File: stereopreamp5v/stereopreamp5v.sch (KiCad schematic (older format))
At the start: 28 parts, among them J1 Conn_Coaxial, J2 Conn_Coaxial, J3 Conn_Coaxial, J4 Conn_Coaxial, U1 TL072

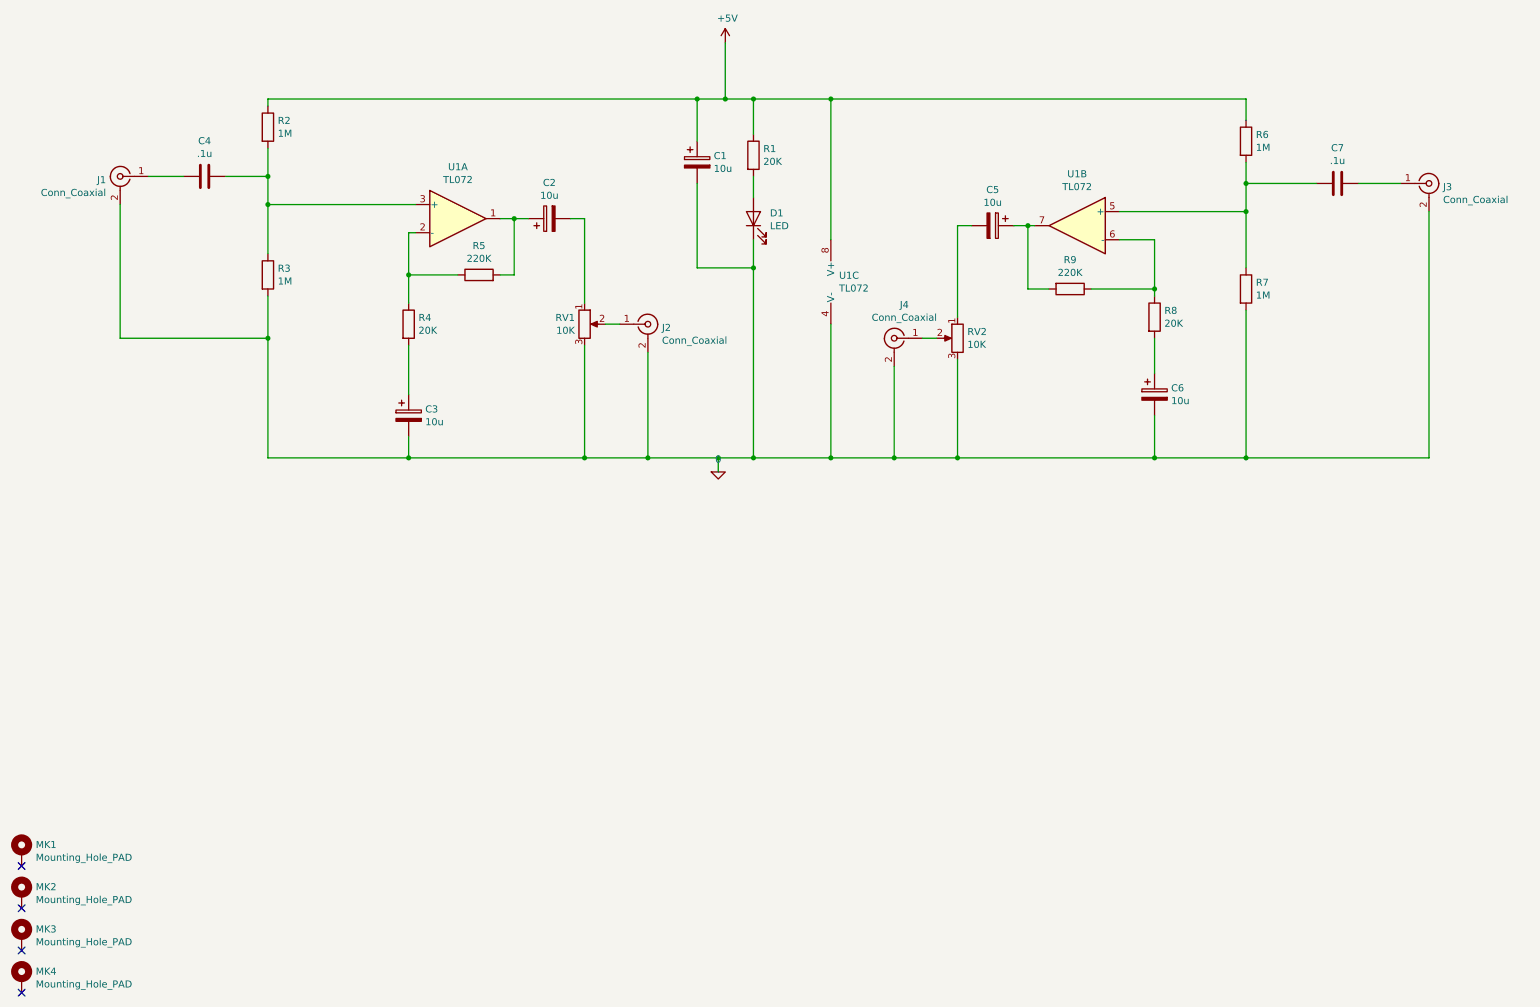
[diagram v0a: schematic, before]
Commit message: replaced input connector
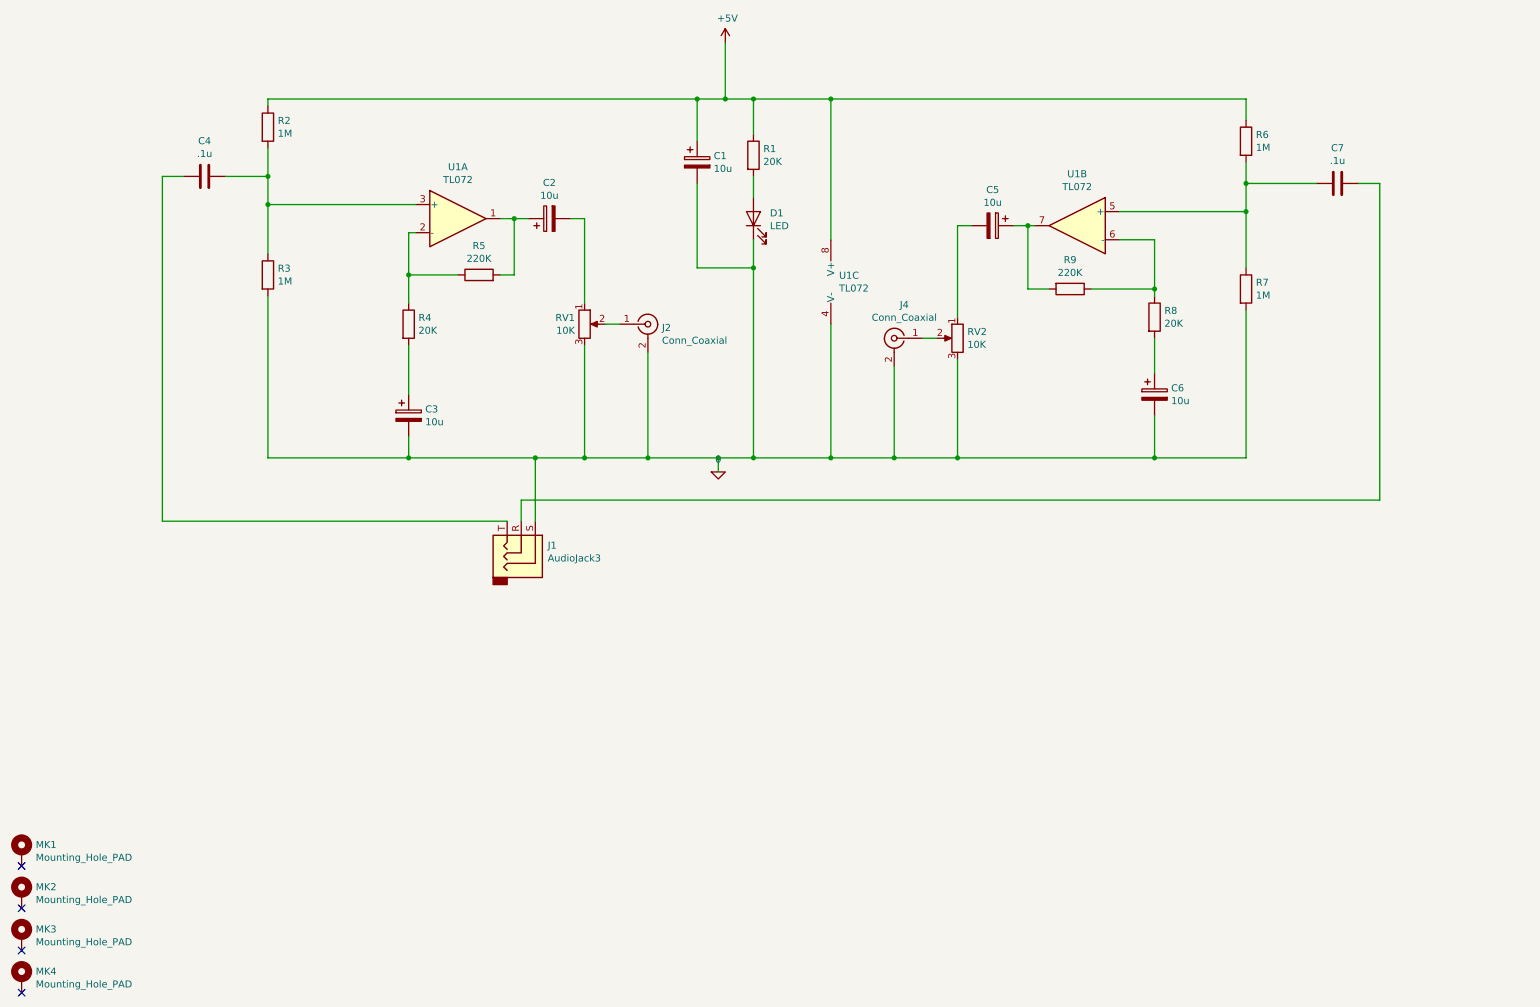
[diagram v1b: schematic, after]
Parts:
- removed J1, J3: Conn_Coaxial, symbol Connector:Conn_Coaxial
- added J1: AudioJack3, symbol Connector:AudioJack3
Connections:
- net 0: now also J1.S
- net at C4.1: now also J1.T
- net at C7.1: now also J1.R
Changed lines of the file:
@@
 NoConn ~ 650  7700
-$Comp
-L Connector:Conn_Coaxial J3
-U 1 1 5E905D21
-P 10650 1950
-F 0 "J3" H 10750 1925 50  0000 L CNN
-F 1 "Conn_Coaxial" H 10750 1834 50  0000 L CNN
-F 2 "" H 10650 1950 50  0001 C CNN
-F 3 " ~" H 10650 1950 50  0001 C CNN
-	1    10650 1950
-	1    0    0    -1
-$EndComp
 $Comp
 L Device:CP C1
@@
 $EndComp
 Wire Wire Line
-	10150 1950 10450 1950
-Wire Wire Line
 	8450 2150 9350 2150
 Wire Wire Line
@@
 Wire Wire Line
 	9350 1950 9350 2150
-Wire Wire Line
-	10650 2150 10650 3900
-Wire Wire Line
-	10650 3900 9350 3900
 Connection ~ 8700 3900
 Wire Wire Line
 	9350 2850 9350 3900
-Connection ~ 9350 3900
 Wire Wire Line
 	9350 3900 8700 3900
@@
 	1    0    0    -1
 $EndComp
-Wire Wire Line
-	1350 2100 1350 3050
-$Comp
-L Connector:Conn_Coaxial J1
-U 1 1 5E904417
-P 1350 1900
-F 0 "J1" H 1450 1875 50  0000 L CNN
-F 1 "Conn_Coaxial" H 1450 1784 50  0000 L CNN
-F 2 "" H 1350 1900 50  0001 C CNN
-F 3 " ~" H 1350 1900 50  0001 C CNN
-	1    1350 1900
-	-1   0    0    -1
-$EndComp
-Wire Wire Line
-	1550 1900 1800 1900
 Connection ~ 2400 1900
 Wire Wire Line
@@
 $EndComp
 Wire Wire Line
-	3400 3900 4650 3900
+	3400 3900 4300 3900
 $Comp
 L Device:R R3
@@
 	5600 3900 5100 3900
 Wire Wire Line
-	1350 3050 2400 3050
-Wire Wire Line
-	2400 3050 2400 2750
-Wire Wire Line
-	2400 3050 2400 3900
-Wire Wire Line
 	2400 3900 3400 3900
-Connection ~ 2400 3050
 Connection ~ 3400 3900
 Wire Wire Line
@@
 Wire Wire Line
 	4150 2200 4250 2200
+$Comp
+L Connector:AudioJack3 J1
+U 1 1 5E91EC0C
+P 4200 4550
+F 0 "J1" V 4228 4738 50  0000 L CNN
+F 1 "AudioJack3" V 4137 4738 50  0000 L CNN
+F 2 "" H 4200 4550 50  0001 C CNN
+F 3 "~" H 4200 4550 50  0001 C CNN
+	1    4200 4550
+	0    1    -1   0
+$EndComp
+Wire Wire Line
+	4300 4350 4300 3900
+Connection ~ 4300 3900
+Wire Wire Line
+	4300 3900 4650 3900
+Wire Wire Line
+	4100 4350 1650 4350
+Wire Wire Line
+	1650 4350 1650 1900
+Wire Wire Line
+	1650 1900 1800 1900
+Wire Wire Line
+	2400 2750 2400 3900
+Wire Wire Line
+	10150 1950 10300 1950
+Wire Wire Line
+	10300 1950 10300 4200
+Wire Wire Line
+	10300 4200 4200 4200
+Wire Wire Line
+	4200 4200 4200 4350
 $EndSCHEMATC
